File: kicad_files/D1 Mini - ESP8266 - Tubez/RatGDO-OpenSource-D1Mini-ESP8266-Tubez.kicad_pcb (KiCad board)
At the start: 2 copper layers, 51.8 x 65.8 mm, 27 parts, among them J1 Screw_Terminal_01x03, J2 Conn_01x11, J3 Screw_Terminal_01x02, Q1 2N7002, Q2 AO3400A, Q3 AO3400A, Q4 AO3400A, U1 WeMos_D1_mini, U2 K7805-500R3

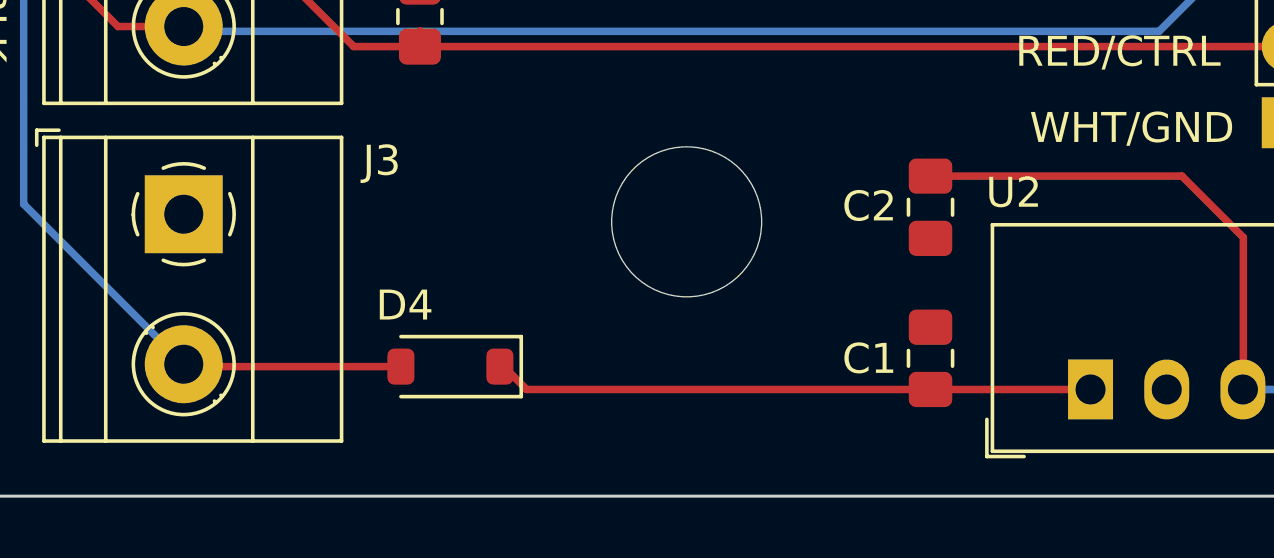
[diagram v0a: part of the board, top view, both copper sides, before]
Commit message: Added 500mA fuse to input power
fuse is expensive on jlcpcb.  need to explore other part numbers., maybe move to 1206 size ptc instead.
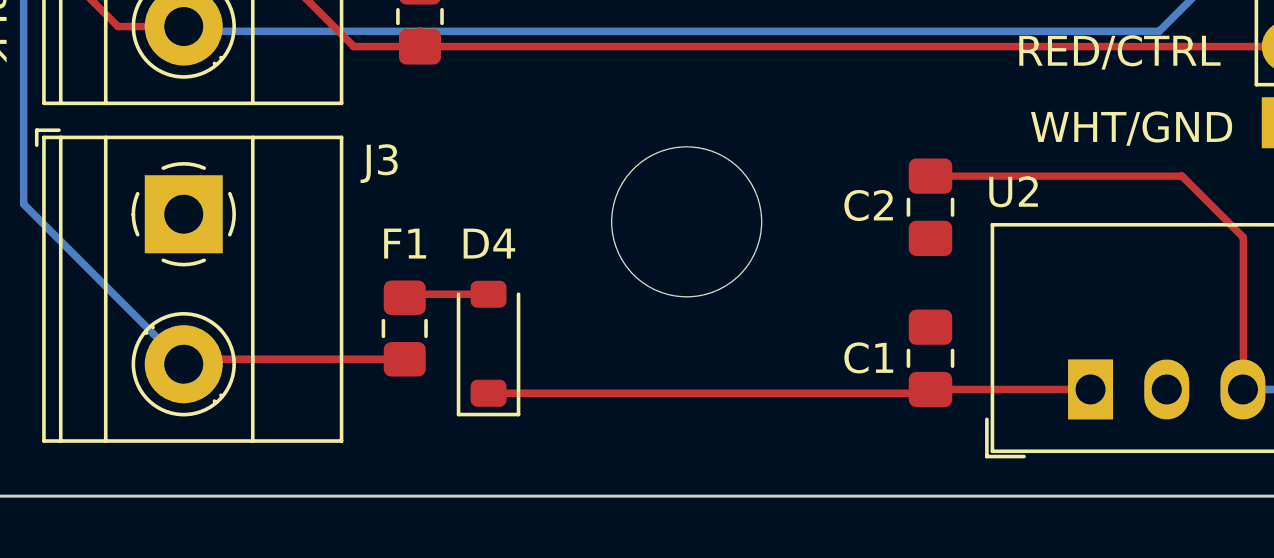
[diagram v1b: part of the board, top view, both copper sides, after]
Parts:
- added F1: 500mA, Fuse:Fuse_0805_2012Metric_Pad1.15x1.40mm_HandSolder, F.Cu at (132.1, 117.3)
- moved D4 1.48 mm to (134.9, 117.9), turned to 90 degrees
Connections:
- D4 pad 2: +12V -> Net-(D4-A)
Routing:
- net Net-(D4-A): track 0.00 -> 2.84 mm
- net +12V: track 112.9 -> 113.5 mm

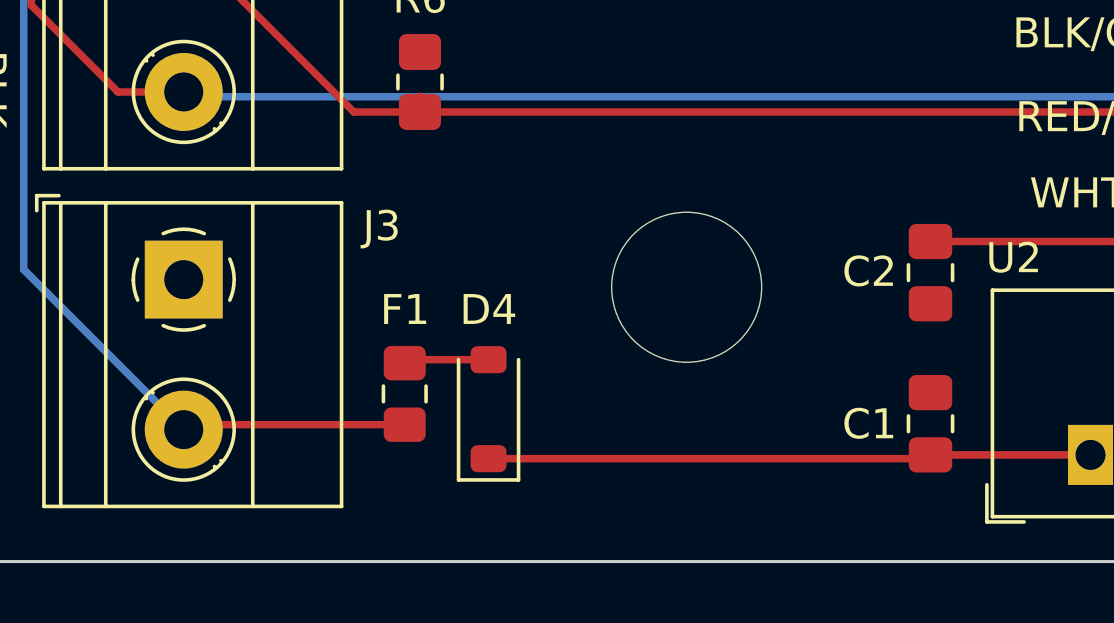
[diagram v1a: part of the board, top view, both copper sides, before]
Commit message: Change to 750mA fuse 1206 package
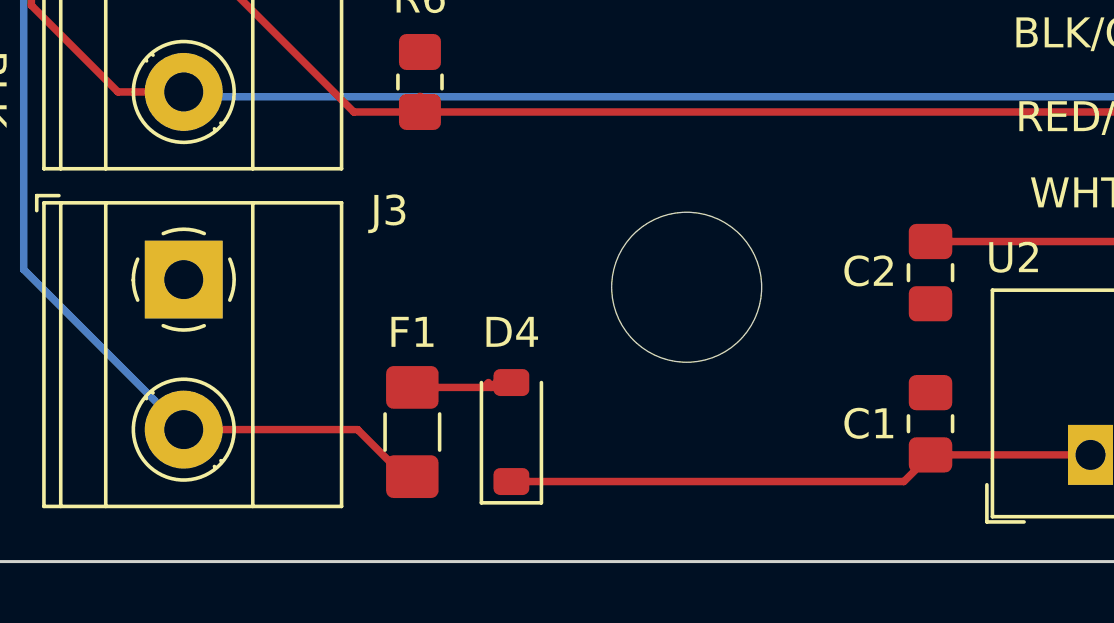
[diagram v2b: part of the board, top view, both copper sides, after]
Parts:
- F1: footprint Fuse:Fuse_0805_2012Metric_Pad1.15x1.40mm_HandSolder -> Fuse:Fuse_1206_3216Metric_Pad1.42x1.75mm_HandSolder
- moved F1 1.30 mm to (132.3, 118.6)
- moved D4 1.08 mm to (135.6, 118.6)
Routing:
- net Net-(D4-A): track 2.84 -> 3.60 mm
- net +12V: track 113.5 -> 114.0 mm

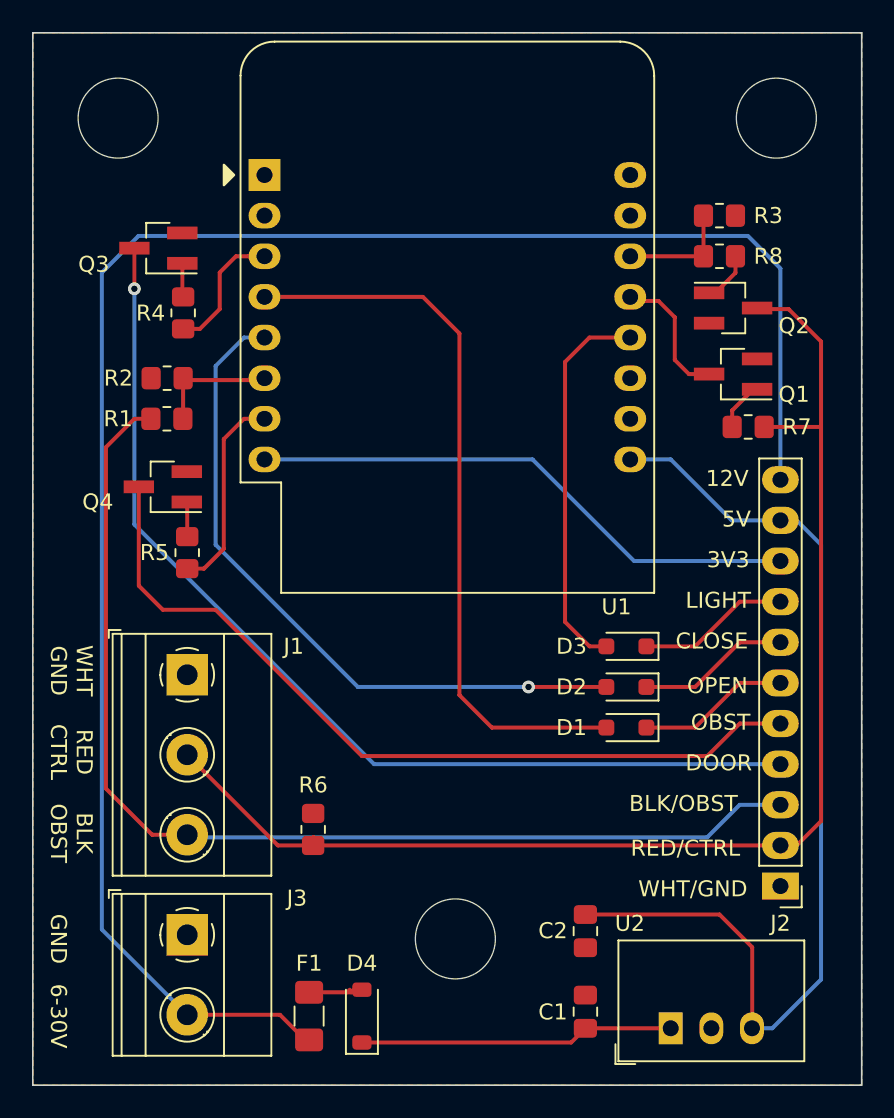
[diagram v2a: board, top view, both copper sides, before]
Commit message: Add 3v3 or 5V jumper for use of different dcdc
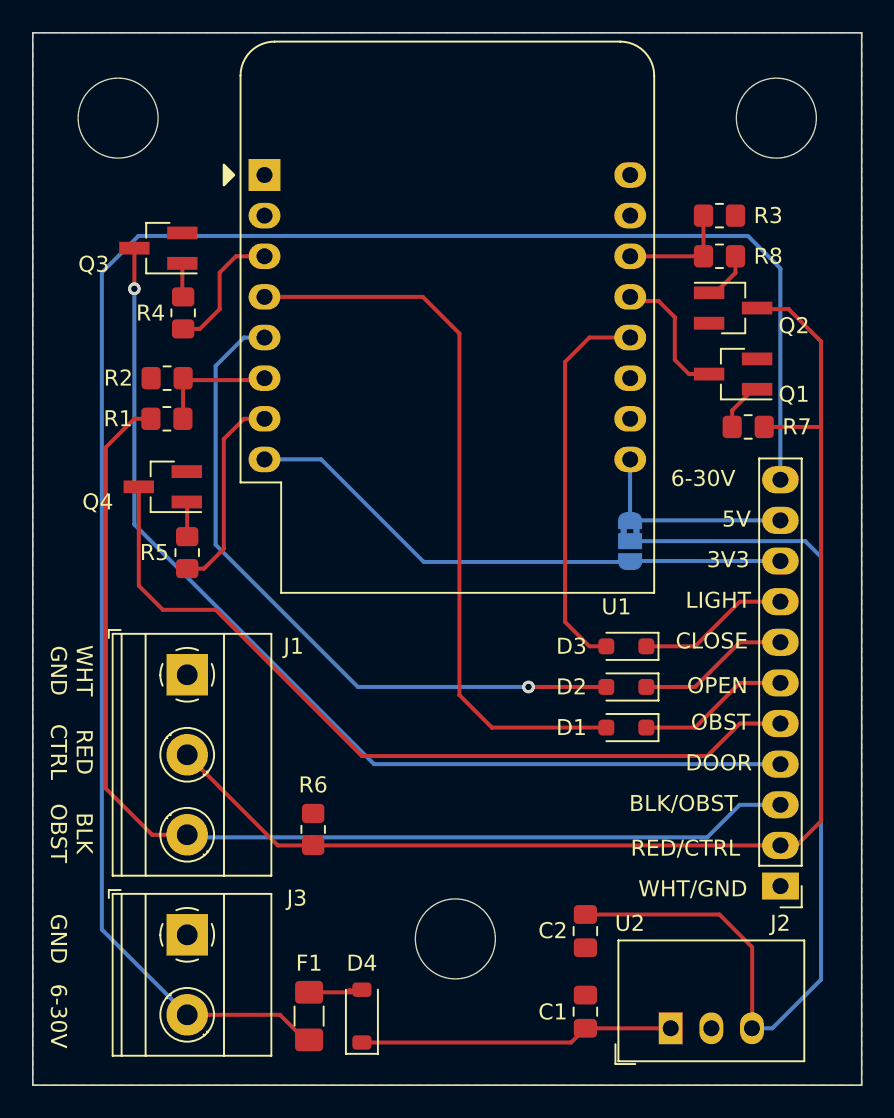
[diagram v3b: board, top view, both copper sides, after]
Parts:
- added JP1: ~, Custom Library:SolderJumper-3_P1.3mm_Bridged2Bar12_RoundedPad1.0x1.5mm_voltjump, B.Cu at (152.4, 88.9)
- F1: value 500mA -> 750mA
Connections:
- C2 pad 1: +5V -> Net-(JP1-C)
- U2 pad 3: +5V -> Net-(JP1-C)
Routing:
- net Net-(JP1-C): track 0.00 -> 60.4 mm
- net +5V: track 61.4 -> 13.2 mm
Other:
- board text removed: "12V"
